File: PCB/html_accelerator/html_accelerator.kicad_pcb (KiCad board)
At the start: 4 copper layers, 129.3 x 104.4 mm, 170 parts, among them J1 Bus_PCI_Express_x16, J2 PCIexpress_bracket, U1 MCS9990, U10 AU6438BS, U11 EMMC_4G, U12 MCS9990, U2 AP1513, U3 CAT24C256YI-GT3, U4 AU6438BS, U5 EMMC_4G, U6 EMMC_4G, U7 EMMC_4G, U8 AU6438BS, U9 AU6438BS, Y1 12MHz, Y2 12MHz, Y3 12MHz, Y4 12MHz, Y5 12MHz

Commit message: routing checkpoint
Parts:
- removed C20, C25: 0.1uF, Capacitor_SMD:C_0805_2012Metric_Pad1.18x1.45mm_HandSolder
- removed FB3, FB4: BLM21PG121SN1D, Resistor_SMD:R_0805_2012Metric_Pad1.20x1.40mm_HandSolder
- moved R7 14.5 mm to (173.7, 130.6), turned to 180 degrees
- moved R10 6.53 mm to (168.1, 127.0)
- moved R9 5.80 mm to (176.8, 138.5)
- moved C5 5.80 mm to (173.7, 138.5)
- moved R14 3.30 mm to (176.8, 108.3), turned to 90 degrees
- moved R11 2.82 mm to (168.0, 120.1)
- moved R16 2.73 mm to (168.0, 116.8)
- moved R12 2.62 mm to (168.0, 113.6)
- moved R13 2.50 mm to (168.0, 110.3)
- moved R28 0.23 mm to (145.2, 65.0)
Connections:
- net Net-(U1A-+1.2VOUT_REG) renamed /PCIE_POWER/1v2_REG
- C10 pad 1: Net-(C10-Pad1) -> /PCIE_POWER/1v2_filt
- C11 pad 1: Net-(C10-Pad1) -> /PCIE_POWER/1v2_filt
- C12 pad 1: Net-(C10-Pad1) -> /PCIE_POWER/1v2_filt
- C21 pad 1: Net-(U1A-+1.2VA_AUX) -> /PCIE_POWER/1v2_filt
- C22 pad 1: Net-(U1A-+1.2VA_AUX) -> /PCIE_POWER/1v2_filt
- C26 pad 1: Net-(U1A-+3.3VA_AUX) -> 3v3_filt
- C27 pad 1: Net-(U1A-+3.3VA_AUX) -> 3v3_filt
- C28 pad 1: Net-(U1A-+3.3VA_AUX) -> 3v3_filt
- C29 pad 1: Net-(U1A-+3.3VA_AUX) -> 3v3_filt
- C30 pad 1: Net-(U1A-+3.3VA_AUX) -> 3v3_filt
- C41 pad 2: Net-(U4-XTAL_OUT) -> GND
- C7 pad 1: Net-(C10-Pad1) -> /PCIE_POWER/1v2_filt
- C8 pad 1: Net-(C10-Pad1) -> /PCIE_POWER/1v2_filt
- C9 pad 1: Net-(C10-Pad1) -> /PCIE_POWER/1v2_filt
- FB1 pad 1: Net-(C10-Pad1) -> /PCIE_POWER/1v2_filt
- U1 pad 109: Net-(C10-Pad1) -> /PCIE_POWER/1v2_filt
- U1 pad 110: Net-(U1A-+3.3VA_AUX) -> 3v3_filt
- U1 pad 111: Net-(U1A-+3.3VA_AUX) -> 3v3_filt
- U1 pad 119: Net-(U1A-+3.3VA_AUX) -> 3v3_filt
- U1 pad 12: Net-(U1A-+1.2VA_AUX) -> /PCIE_POWER/1v2_filt
- U1 pad 121: Net-(C10-Pad1) -> /PCIE_POWER/1v2_filt
- U1 pad 15: Net-(U1A-+1.2VA_AUX) -> /PCIE_POWER/1v2_filt
- U1 pad 16: Net-(U1A-+3.3VA_AUX) -> 3v3_filt
- U1 pad 19: Net-(U1A-+3.3VA_AUX) -> 3v3_filt
- U1 pad 20: Net-(C10-Pad1) -> /PCIE_POWER/1v2_filt
- U1 pad 33: Net-(C10-Pad1) -> /PCIE_POWER/1v2_filt
- U1 pad 51: Net-(U1A-+3.3VA_AUX) -> 3v3_filt
- U1 pad 52: Net-(U1A-+3.3VA_AUX) -> 3v3_filt
- U1 pad 58: Net-(C10-Pad1) -> /PCIE_POWER/1v2_filt
- U1 pad 6: Net-(U1A-+1.2VA_AUX) -> /PCIE_POWER/1v2_filt
- U1 pad 80: Net-(C10-Pad1) -> /PCIE_POWER/1v2_filt
- U1 pad 83: Net-(U1A-+3.3VA_AUX) -> 3v3_filt
- U1 pad 84: Net-(U1A-+3.3VA_AUX) -> 3v3_filt
- U1 pad 90: Net-(U1A-+3.3VA_AUX) -> 3v3_filt
- U1 pad 91: Net-(U1A-+3.3VA_AUX) -> 3v3_filt
- U1 pad 98: Net-(C10-Pad1) -> /PCIE_POWER/1v2_filt
- U12 pad 100: GND -> unconnected-(U12D-USB0_PWR_EN_N-Pad100)
- U12 pad 103: GND -> unconnected-(U12D-USB1_PWR_EN_N-Pad103)
- U12 pad 123: GND -> unconnected-(U12D-USB2_PWR_EN_N-Pad123)
- U12 pad 126: GND -> unconnected-(U12D-USB3_PWR_EN_N-Pad126)
- U12 pad 13: GND -> unconnected-(U12C-PCIE_TXDP-Pad13)
- U12 pad 14: GND -> unconnected-(U12C-PCIE_TXDN-Pad14)
- U12 pad 22: GND -> unconnected-(U12C-PCIE_CLKREQ_N-Pad22)
- U12 pad 23: GND -> unconnected-(U12C-PCIE_WAKE_N-Pad23)
- U12 pad 3: GND -> unconnected-(U12A-+1.2VOUT_REG-Pad3)
- U12 pad 62: GND -> unconnected-(U12E-JTAG_TDO-Pad62)
- U12 pad 65: GND -> unconnected-(U12B-GPIO12/CSA_N-Pad65)
- U12 pad 66: GND -> unconnected-(U12B-GPIO13/CSB_N-Pad66)
- U12 pad 67: GND -> unconnected-(U12B-GPIO14/CSC_N-Pad67)
- U12 pad 68: GND -> unconnected-(U12B-GPIO15/CSD_N-Pad68)
- U12 pad 7: GND -> unconnected-(U12C-REXT-Pad7)
- U12 pad 71: GND -> unconnected-(U12B-GPIO16/RESET-Pad71)
- U12 pad 72: GND -> unconnected-(U12B-GPIO17/IOW_N-Pad72)
- U12 pad 73: GND -> unconnected-(U12B-GPIO18/IOR_N-Pad73)
- U12 pad 75: GND -> unconnected-(U12B-GPIO19/A0-Pad75)
- U12 pad 76: GND -> unconnected-(U12B-GPIO20/A1-Pad76)
- U12 pad 77: GND -> unconnected-(U12B-GPIO21/A2-Pad77)
- U12 pad 82: GND -> unconnected-(U12B-USB0_XSCO-Pad82)
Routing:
- net +5V: track 75.2 -> 315.6 mm
- net Net-(U1E-EE_SCL): track 0.00 -> 100.7 mm, vias 0 -> 4
- net Net-(U1E-EE_SDA): track 0.00 -> 99.5 mm, vias 0 -> 4
- net +3V3: track 0.00 -> 81.6 mm, vias 0 -> 11
- net 3v3_filt: track 0.00 -> 61.2 mm, vias 0 -> 29
- net +12V: track 101.1 -> 160.8 mm, vias 2 -> 37
- net /PCIE_POWER/1v2_filt: track 0.00 -> 53.9 mm, vias 0 -> 17
- net +3V0: track 0.00 -> 53.5 mm, vias 0 -> 2
- net /PCIE_Slot/PCIE_WAKE: track 0.00 -> 36.2 mm, vias 0 -> 4
- net Net-(J1-~{PRSNT1}): track 0.00 -> 33.6 mm, vias 0 -> 2
- net Net-(J1-~{PERST}): track 0.00 -> 32.1 mm, vias 0 -> 3
- net Net-(J1-~{WAKE}): track 0.00 -> 31.8 mm, vias 0 -> 2
- net Net-(U1E-OTG_EN_N): track 0.00 -> 31.8 mm, vias 0 -> 2
- net +1V2: track 0.00 -> 24.3 mm
- net /PCIE_Slot/PCIE_CLKreq: track 0.00 -> 22.6 mm, vias 0 -> 2
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- added copper zone on In1.Cu, net +12V
- added copper zone on In1.Cu, net /PCIE_POWER/1v2_filt
- added copper zone on In2.Cu, net 3v3_filt
- added copper zone on F.Cu, net Net-(D1-K)

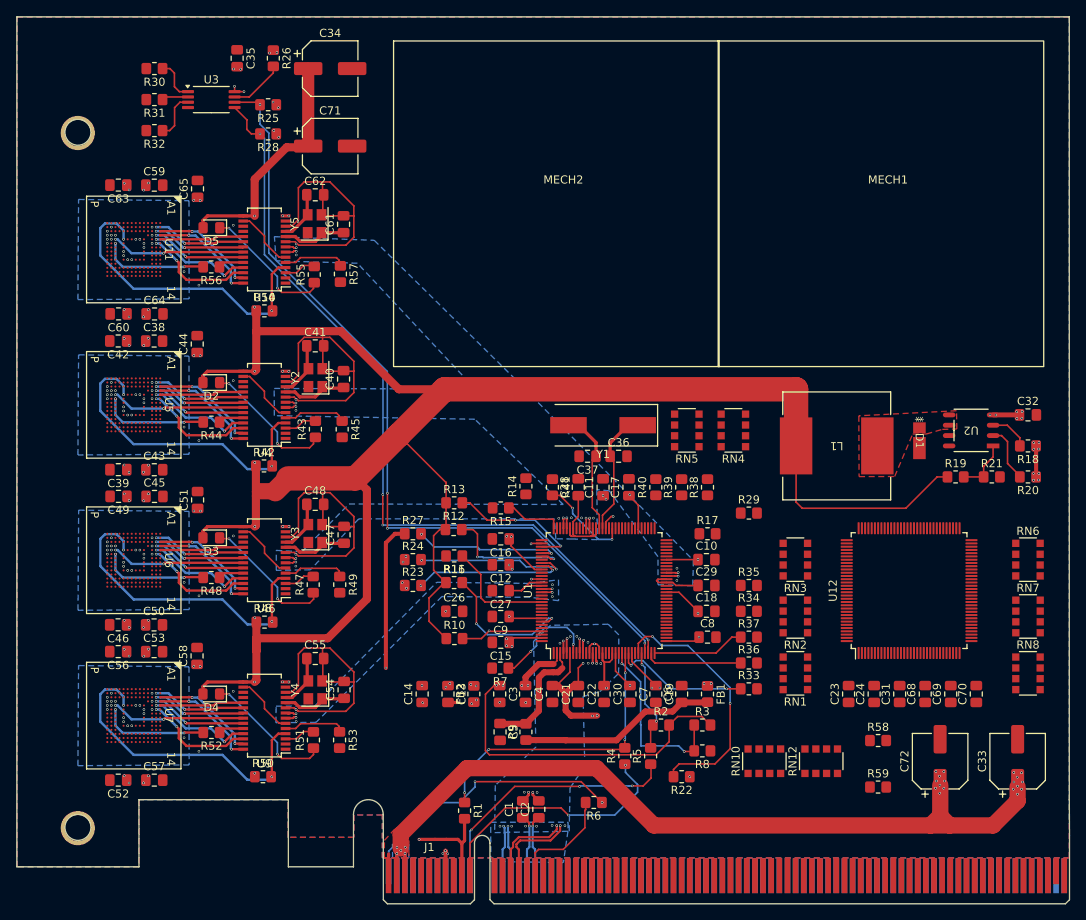
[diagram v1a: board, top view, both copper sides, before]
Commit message: nearly done routing
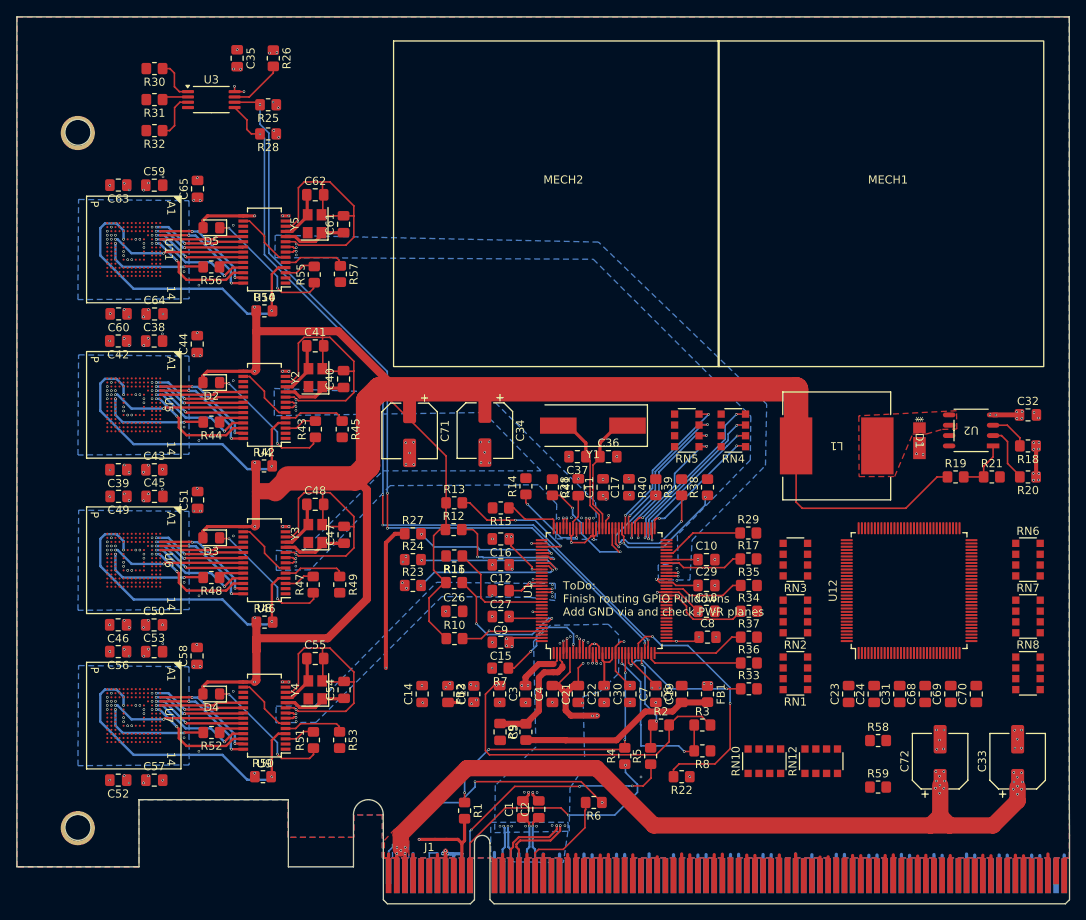
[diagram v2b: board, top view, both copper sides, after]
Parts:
- moved C34 48.4 mm to (171.8, 101.4), turned to -90 degrees
- moved C71 36.3 mm to (162.6, 101.5), turned to -90 degrees
- moved R17 5.91 mm to (204.2, 117.2)
- moved R29 2.45 mm to (204.2, 114.0)
- moved C36 1.25 mm to (187.0, 104.6)
- moved C37 1.25 mm to (183.2, 104.6)
- moved Y1 1.25 mm to (185.1, 100.8)
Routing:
- net GND: track 141.5 -> 313.7 mm, vias 82 -> 150
- net 90_USB3_D_N: track 69.8 -> 93.0 mm
- net 90_USB3_D_P: track 68.3 -> 91.5 mm
- net Net-(RN4-R4.1): track 0.00 -> 22.1 mm, vias 0 -> 2
- net Net-(RN4-R3.1): track 0.00 -> 20.8 mm, vias 0 -> 2
- net Net-(RN4-R2.1): track 0.00 -> 19.6 mm, vias 0 -> 2
- net Net-(RN5-R4.1): track 0.00 -> 19.4 mm, vias 0 -> 2
- net Net-(RN5-R2.1): track 0.00 -> 19.4 mm, vias 0 -> 2
- net Net-(RN5-R3.1): track 0.00 -> 18.2 mm, vias 0 -> 2
- net +5V: track 315.6 -> 298.3 mm
- net Net-(RN4-R1.1): track 0.00 -> 15.9 mm, vias 0 -> 2
- net Net-(RN5-R1.1): track 0.00 -> 15.3 mm, vias 0 -> 2
- net Net-(U1B-GPIO19/A0): track 0.00 -> 15.3 mm, vias 0 -> 2
- net Net-(U1B-GPIO20/A1): track 0.00 -> 14.3 mm, vias 0 -> 2
- net Net-(U1E-MODE_SEL1): track 0.00 -> 11.2 mm
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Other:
- board text added: "ToDo: Finish routing GPIO Pulldowns Add GND via and check PWR planes"
